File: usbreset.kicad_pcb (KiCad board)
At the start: 2 copper layers, 0 parts

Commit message: Initial PCB layout
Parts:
- added C1: 2000pF, Capacitor_SMD:C_0603_1608Metric, F.Cu at (161.9, 101.1)
- added J1: USB_C_PowerSource, Connector_USB-Custom:USB_C_Receptacle_Amphenol_10137065, F.Cu at (170.2, 102.9)
- added J2: USB_C_PowerSink, Connector_USB-Custom:USB_C_Receptacle_Amphenol_10137065, F.Cu at (134.6, 102.9)
- added J3: USB3_A_Plug, Connector_USB-Custom:USB_A_Plug_Amphenol_GSB3164x1CEU, F.Cu at (152.4, 111.5)
- added J4: USB3_A_Receptacle, Connector_USB-Custom:USB_A_Receptacle_Amphenol_10117835, F.Cu at (152.4, 89.5)
- added Q1: SI2393DS, Package_TO_SOT_SMD:SOT-23, F.Cu at (160.9, 105.1)
- added R1: 5.1k, Resistor_SMD:R_0603_1608Metric_Pad1.05x0.95mm_HandSolder, F.Cu at (152.3, 98.6)
- added R2: 40k, Resistor_SMD:R_0603_1608Metric_Pad1.05x0.95mm_HandSolder, F.Cu at (158.1, 99.5)
- added R3: 1M, Resistor_SMD:R_0603_1608Metric_Pad1.05x0.95mm_HandSolder, F.Cu at (158.1, 103.1)
- added R4: 1.5M, Resistor_SMD:R_0603_1608Metric_Pad1.05x0.95mm_HandSolder, F.Cu at (160.0, 101.2)
- added SW1: EN_USBA, Button_Switch_SMD-Custom:SW_SPDT_MSS3-V-T_R, F.Cu at (152.4, 102.3)
- added SW2: SW_Push, Button_Switch_SMD:SW_Push_1P1T_NO_CK_KSC7xxJ, B.Cu at (152.4, 102.9)
- added SW3: SW_Push, Connector_PinHeader_2.54mm:PinHeader_1x02_P2.54mm_Vertical, F.Cu at (145.0, 101.6)
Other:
- board outline added: 39.1 x 22.9 mm
- net class Default: clearance 0.2 -> 0.16; trace_width 0.25 -> 0.1524; via_dia 0.8 -> 0.381; via_drill 0.4 -> 0.254
- net class Power added: clearance 0.21, trace_width 0.2032, via_dia 0.508, via_drill 0.3302
- rule trace_clearance: 0.2 -> 0.16
- rule trace_min: 0.2 -> 0.1524
- rule via_min_drill: 0.3 -> 0.254
- rule via_min_size: 0.4 -> 0.381

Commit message: More tweaks
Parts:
- moved C1 1.14 mm to (160.9, 101.6)
- moved R2 1.14 mm to (157.1, 100.0)
- moved R3 1.14 mm to (157.1, 103.6)
- moved R4 1.14 mm to (159.0, 101.7)
- moved Q1 1.03 mm to (159.9, 105.3)
- moved R1 0.85 mm to (151.5, 98.9)
- moved SW1 0.79 mm to (151.6, 102.5)
- moved SW3 0.38 mm to (145.4, 101.6)
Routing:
- net Net-(C1-Pad2): track 0.00 -> 8.38 mm
- net VBUS: track 0.00 -> 3.81 mm
- net Net-(R1-Pad2): track 0.00 -> 1.81 mm
- net Net-(J2-PadA10): vias 0 -> 1
- net Net-(J1-PadB8): vias 0 -> 2
- net Net-(J1-PadB7): vias 0 -> 2
- net Net-(J1-PadB6): vias 0 -> 2
- net Net-(J1-PadB5): vias 0 -> 2
- net Net-(J1-PadB3): vias 0 -> 2
- net Net-(J1-PadB2): vias 0 -> 2
- net Net-(J1-PadB11): vias 0 -> 3
- net Net-(J1-PadB10): vias 0 -> 3
- net Net-(J1-PadA8): vias 0 -> 2
- net Net-(J1-PadA7): vias 0 -> 3
- net Net-(J1-PadA6): vias 0 -> 3
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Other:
- net class Power: clearance 0.21 -> 0.16

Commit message: Route most connections
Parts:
- added R5: 0, Resistor_SMD:R_0603_1608Metric_Pad1.05x0.95mm_HandSolder, F.Cu at (160.8, 94.5)
- J1, J2, J3, J4, SW3: moved to B.Cu
- moved J3 26.8 mm to (177.8, 102.9), turned to 270 degrees
- moved SW3 24.4 mm to (169.2, 96.5), turned to 90 degrees
- moved J2 20.5 mm to (153.4, 111.2), turned to 180 degrees
- moved J1 18.8 mm to (153.4, 94.5), turned to 0 degrees
- moved J4 18.6 mm to (139.4, 102.9), turned to 90 degrees
- moved SW2 15.5 mm to (167.9, 102.9), turned to 90 degrees
- moved R1 15.2 mm to (164.7, 106.4)
- moved SW1 15.0 mm to (164.6, 110.0)
- moved R3 11.8 mm to (168.4, 100.3), turned to 0 degrees
- moved R2 11.4 mm to (168.4, 98.8), turned to 0 degrees
- moved R4 7.19 mm to (165.9, 99.6)
- moved Q1 6.02 mm to (161.8, 99.6)
- moved C1 4.00 mm to (164.3, 99.6)
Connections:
- J1 pad A10: Net-(J1-PadA10) -> /RX2-
- J1 pad A11: Net-(J1-PadA11) -> /RX2+
- J1 pad A2: Net-(J1-PadA2) -> /TX1+
- J1 pad A3: Net-(J1-PadA3) -> /TX1-
- J1 pad A5: Net-(J1-PadA5) -> /CC1
- J1 pad A6: Net-(J1-PadA6) -> /D+
- J1 pad A7: Net-(J1-PadA7) -> /D-
- J1 pad A8: Net-(J1-PadA8) -> /SBU1
- J1 pad B10: Net-(J1-PadB10) -> /RX1-
- J1 pad B11: Net-(J1-PadB11) -> /RX1+
- J1 pad B2: Net-(J1-PadB2) -> /TX2+
- J1 pad B3: Net-(J1-PadB3) -> /TX2-
- J1 pad B5: Net-(J1-PadB5) -> /CC2
- J1 pad B6: Net-(J1-PadB6) -> /D+
- J1 pad B7: Net-(J1-PadB7) -> /D-
- J1 pad B8: Net-(J1-PadB8) -> /SBU2
- J2 pad A10: Net-(J2-PadA10) -> /RX1-
- J2 pad A11: Net-(J1-PadA11) -> /RX1+
- J2 pad A2: Net-(J1-PadA2) -> /TX2+
- J2 pad A3: Net-(J1-PadA3) -> /TX2-
- J2 pad A5: Net-(J1-PadA5) -> /CC2
- J2 pad A6: Net-(J1-PadA6) -> /D+
- J2 pad A7: Net-(J1-PadA7) -> /D-
- J2 pad A8: Net-(J1-PadA8) -> /SBU2
- J2 pad B10: Net-(J1-PadB10) -> /RX2-
- J2 pad B11: Net-(J1-PadB11) -> /RX2+
- J2 pad B2: Net-(J1-PadB2) -> /TX1+
- J2 pad B3: Net-(J1-PadB3) -> /TX1-
- J2 pad B5: Net-(J1-PadB5) -> /CC1
- J2 pad B6: Net-(J1-PadB6) -> /D+
- J2 pad B7: Net-(J1-PadB7) -> /D-
- J2 pad B8: Net-(J1-PadB8) -> /SBU1
- J3 pad 2: Net-(J1-PadA7) -> /D-
- J3 pad 3: Net-(J1-PadA6) -> /D+
- J3 pad 5: Net-(J1-PadB10) -> /RX1-
- J3 pad 6: Net-(J1-PadB11) -> /RX1+
- J3 pad 8: Net-(J1-PadA3) -> /TX1-
- J3 pad 9: Net-(J1-PadA2) -> /TX1+
- J4 pad 2: Net-(J1-PadA7) -> /D-
- J4 pad 3: Net-(J1-PadA6) -> /D+
- J4 pad 5: Net-(J1-PadB10) -> /RX1-
- J4 pad 6: Net-(J1-PadB11) -> /RX1+
- J4 pad 8: Net-(J1-PadA3) -> /TX1-
- J4 pad 9: Net-(J1-PadA2) -> /TX1+
- SW1 pad 1: Net-(J1-PadA5) -> /CC1
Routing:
- net SHIELD: track 0.00 -> 118.8 mm
- net /VBUS_SINK: track 0.00 -> 33.1 mm, vias 0 -> 1
- net /D-: track 0.00 -> 23.1 mm, vias 0 -> 5
- net /D+: track 0.00 -> 23.0 mm, vias 0 -> 3
- net VBUS: track 3.81 -> 23.0 mm, vias 0 -> 1
- net /TX1+: track 0.00 -> 16.9 mm, vias 0 -> 3
- net /TX1-: track 0.00 -> 16.6 mm, vias 0 -> 2
- net /RX1+: track 0.00 -> 15.3 mm, vias 0 -> 2
- net /RX1-: track 0.00 -> 15.1 mm, vias 0 -> 2
- net Net-(R2-Pad2): track 0.00 -> 11.6 mm, vias 0 -> 2
- net /RX2+: track 0.00 -> 6.98 mm, vias 0 -> 2
- net /TX2+: track 0.00 -> 6.86 mm, vias 0 -> 2
- net /SBU2: track 0.00 -> 6.86 mm, vias 0 -> 2
- net /SBU1: track 0.00 -> 6.82 mm, vias 0 -> 2
- net /RX2-: track 0.00 -> 6.73 mm, vias 0 -> 2
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- added copper zone on B.Cu, net GND
- added copper zone on F.Cu, net GND
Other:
- board size 39.1 x 22.9 mm -> 39.4 x 20.3 mm
- net class Default: clearance 0.16 -> 0.1524
- net class Shield added: clearance 0.16, trace_width 0.254, via_dia 0.508, via_drill 0.3302
- rule trace_clearance: 0.16 -> 0.1524
- board text added: "Sink"
- board text added: "Source"

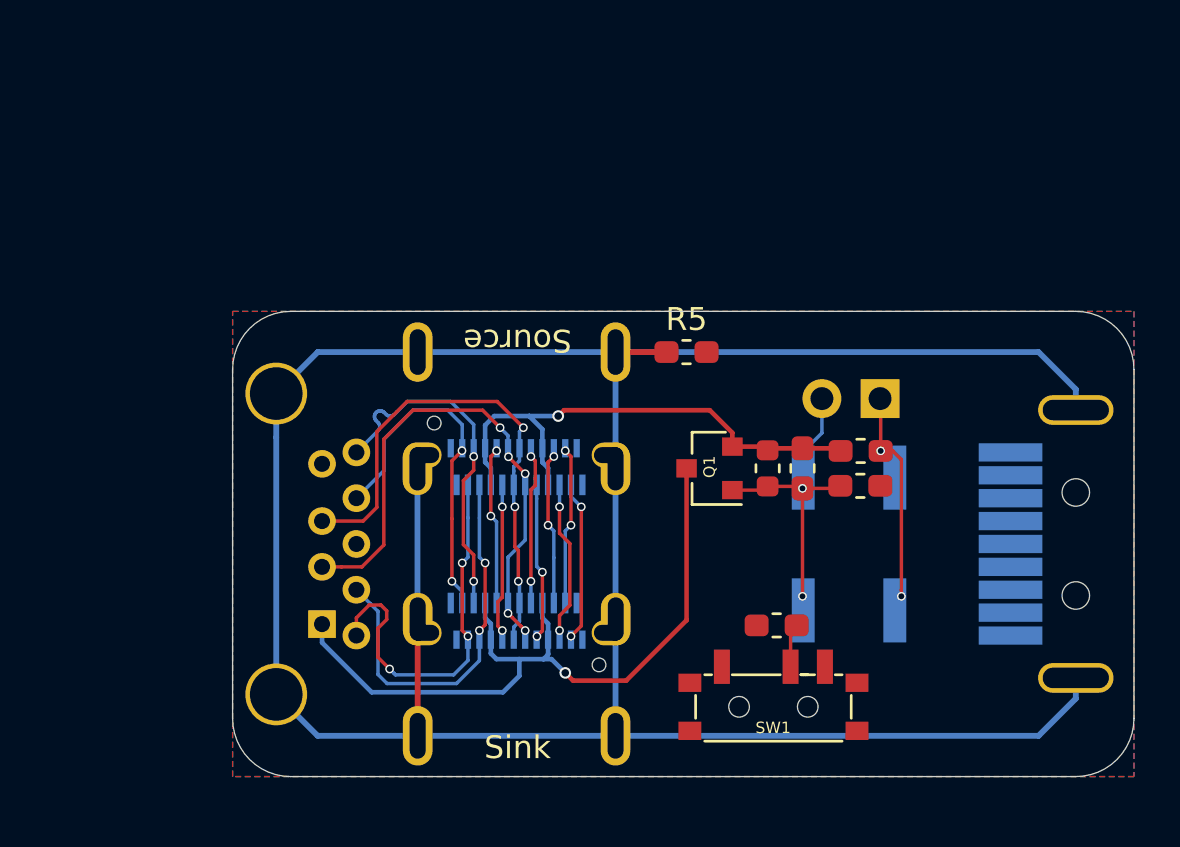
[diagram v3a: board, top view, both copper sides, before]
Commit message: Finish 1st routing pass, add 3D preview
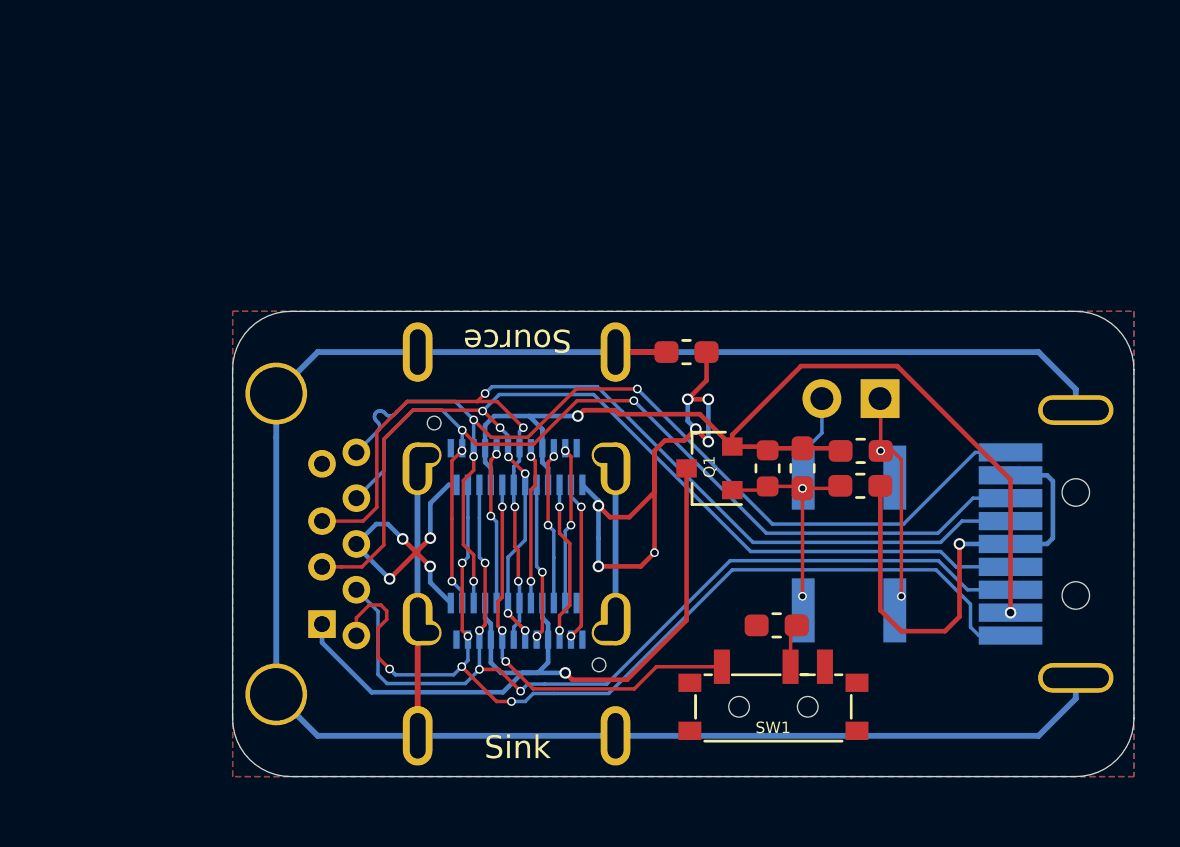
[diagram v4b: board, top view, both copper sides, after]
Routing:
- net GND: track 0.00 -> 60.9 mm, vias 0 -> 12
- net /TX1+: track 16.9 -> 45.6 mm, vias 3 -> 5
- net /RX1-: track 15.1 -> 43.6 mm, vias 2 -> 4
- net /RX1+: track 15.3 -> 43.2 mm, vias 2 -> 4
- net /D+: track 23.0 -> 49.8 mm, vias 3 -> 4
- net /TX1-: track 16.6 -> 43.3 mm, vias 2 -> 4
- net /D-: track 23.1 -> 49.6 mm, vias 5 -> 6
- net VBUS: track 23.0 -> 44.4 mm, vias 1 -> 2
- net /CC1: track 6.52 -> 17.9 mm, vias 2 -> 3
- net SHIELD: track 118.8 -> 108.6 mm
- net /VBUS_SINK: track 33.1 -> 34.0 mm

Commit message: Improve GND routing
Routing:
- net GND: track 60.9 -> 144.6 mm, vias 12 -> 32
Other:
- board text added: "@serverwentdown usbreset v1"
